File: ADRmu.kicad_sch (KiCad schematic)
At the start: 7 parts, among them J1 DIN41612_02x16_AC_EvenPins, J2 10Vf, J3 10Vs, J4 ADR, J6 LoSense, J7 GNDf

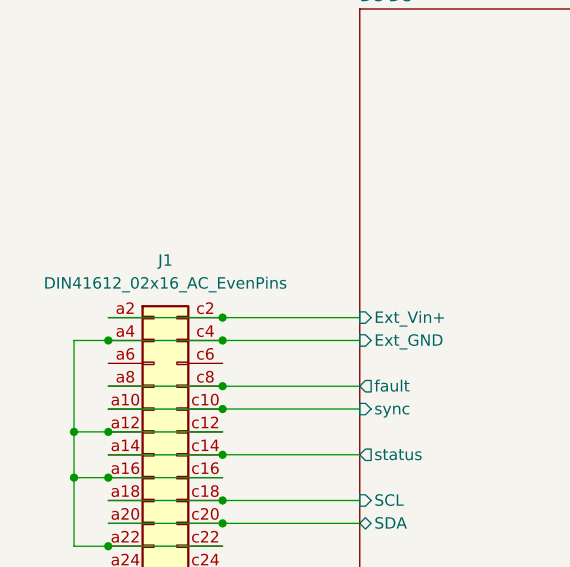
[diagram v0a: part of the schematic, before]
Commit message: schematics updated to rev.2
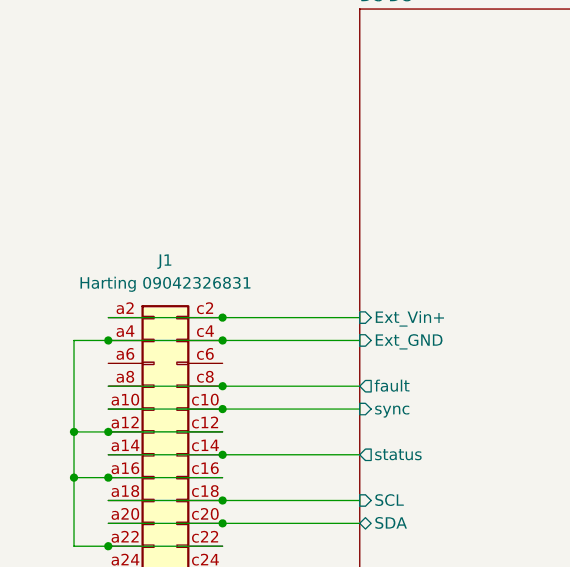
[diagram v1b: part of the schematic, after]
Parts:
- J1: value DIN41612_02x16_AC_EvenPins -> Harting 09042326831
- J2, J3, J4, J6, J7: now left out of the parts list
- SYM101: value SYM_Earth_Protective_Large -> OSMU; now left out of the parts list
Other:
- company: (none) -> RPG
- title: (none) -> Parent schematic

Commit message: asdf
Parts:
- added D101: SMAJ10CA-13-F, Diode_SMD:D_SMA, symbol Device:D_TVS
- renumbered J1 to J101, J2 to J102, J3 to J103, J4 to J104, J6 to J105, J7 to J106
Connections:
- net DC-DC/GNDf: now also D101.1 (A1)
- net ref/10Vforce: now also D101.2 (A2)

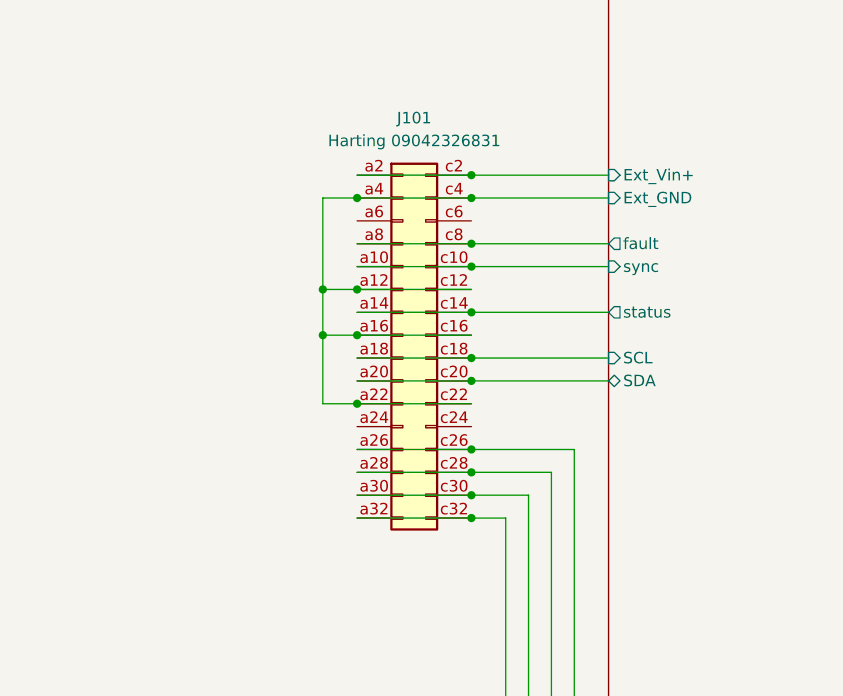
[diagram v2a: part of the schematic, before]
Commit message: adding prec resistor alternatives
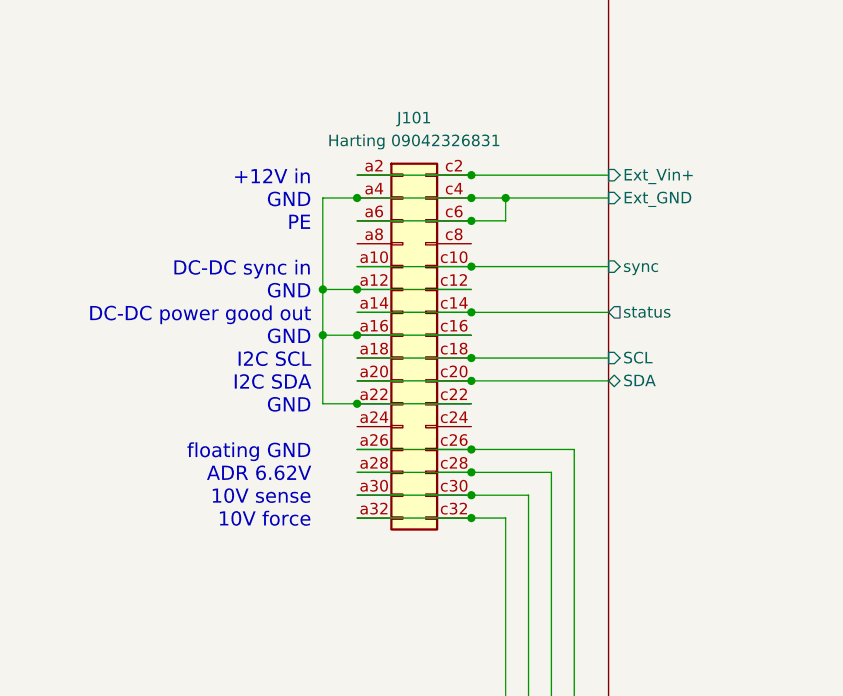
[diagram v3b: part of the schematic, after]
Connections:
- net DC-DC/Ext_GND: now also J101.a6 (Pin_a6), J101.c6 (Pin_c6)
- net DC-DC/fault: no longer names the net of J101.a8 (Pin_a8)
- net DC-DC/fault: no longer J101.c8 (Pin_c8)
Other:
- sheet DC-DC ports: added none; removed fault
- note added: "+12V in GND PE DC-DC sync in GND DC-DC power good out GND I2C SCL I2C SDA GND floating GND ADR 6.62V 10V sense 10V force"

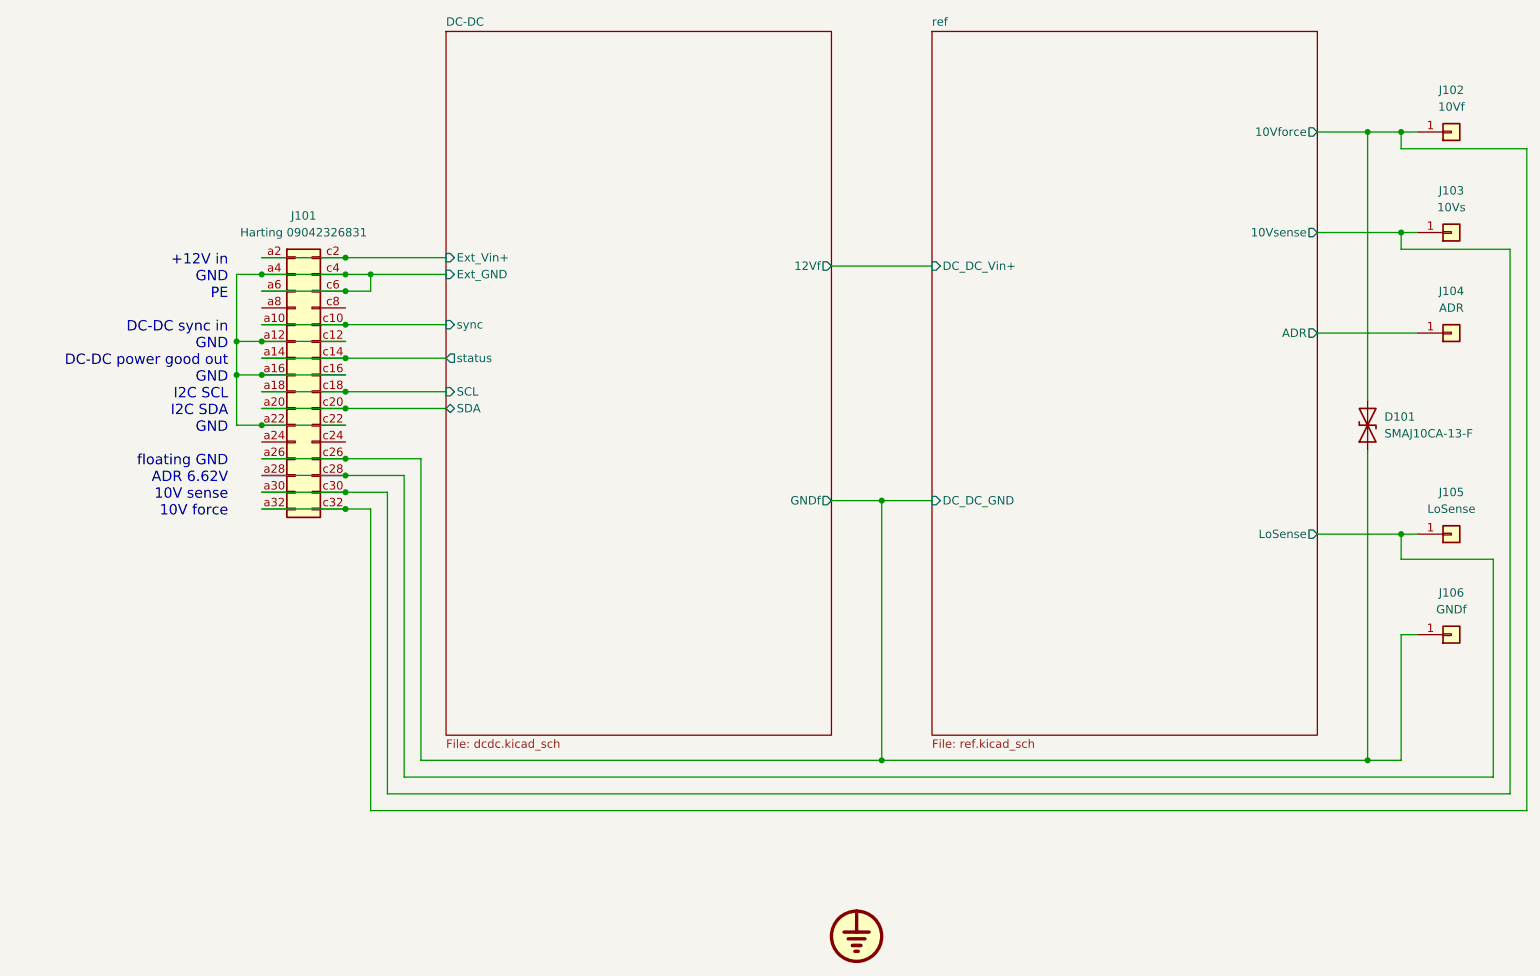
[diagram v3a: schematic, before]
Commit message: goodbye proto area, hello resistor networks
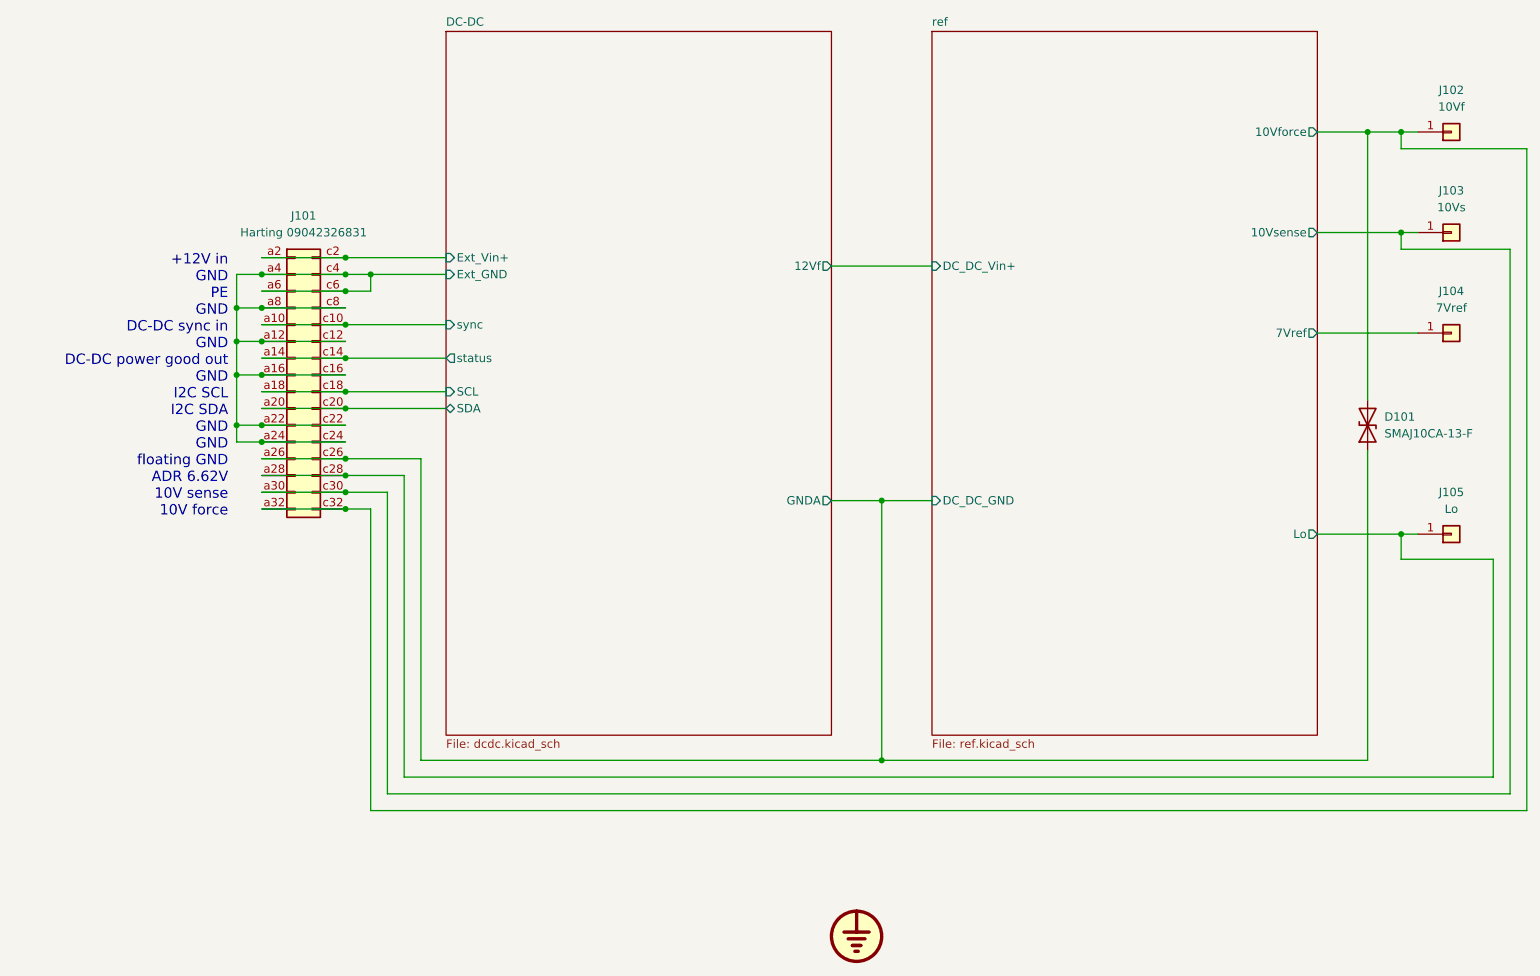
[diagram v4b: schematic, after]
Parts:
- removed J106: GNDf, Connector_Wire:SolderWire-1sqmm_1x01_D1.4mm_OD3.9mm, symbol Connector_Generic:Conn_01x01
- J104: value ADR -> 7Vref
- J105: value LoSense -> Lo
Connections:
- net DC-DC/Ext_GND: now also J101.a24 (Pin_a24), J101.a8 (Pin_a8), J101.c24 (Pin_c24), J101.c8 (Pin_c8)
- net DC-DC/GNDf renamed DC-DC/GNDA
- net ref/ADR renamed ref/7Vref
- net ref/LoSense renamed ref/Lo
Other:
- sheet DC-DC ports: added GNDA; removed GNDf
- sheet ref ports: added 7Vref, Lo; removed ADR, LoSense
- note added: "+12V in GND PE GND DC-DC sync in GND DC-DC power good out GND I2C SCL I2C SDA GND GND floating GND ADR 6.62V 10V sense 10V force"
- note removed: "+12V in GND PE DC-DC sync in GND DC-DC power good out GND I2C SCL I2C SDA GND floating GND ADR 6.62V 10V sense 10V force"

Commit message: Rev 0.3
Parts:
- removed D101: SMAJ10CA-13-F, Diode_SMD:D_SMA, symbol Device:D_TVS
- added D101: SMAJ11A‎, Diode_SMD:D_SMA, symbol Device:D_Zener
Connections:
- net DC-DC/GNDA: now also D101.2 (A)
- net ref/10Vforce: now also D101.1 (K)
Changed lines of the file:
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@@
   (title_block
     (title "Parent schematic")
-    (date "2022-02-02")
-    (rev "0.2")
+    (date "2022-02-11")
+    (rev "0.3")
     (company "RPG")
     (comment 1 "All resistors 0.1% MF unless otherwise noted")
@@
     (at 50.8 114.3 0)
     (effects (font (size 1.5748 1.5748)) (justify right bottom))
+  )
+  (symbol (lib_id "Device:D_Zener") (at 223.52 100.33 270) (unit 1)
+    (in_bom yes) (on_board yes) (fields_autoplaced)
+    (property "Reference" "D101" (id 0) (at 226.06 99.0599 90)
+      (effects (font (size 1.27 1.27)) (justify left))
+    )
+    (property "Value" "SMAJ11A‎" (id 1) (at 226.06 101.5999 90)
+      (effects (font (size 1.27 1.27)) (justify left))
+    )
+    (property "Footprint" "Diode_SMD:D_SMA" (id 2) (at 223.52 100.33 0)
+      (effects (font (size 1.27 1.27)) hide)
+    )
+    (property "Datasheet" "~" (id 3) (at 223.52 100.33 0)
+      (effects (font (size 1.27 1.27)) hide)
+    )
+    (pin "1")
+    (pin "2")
   )
   (symbol (lib_id "Connector_Generic:Conn_01x01") (at 236.22 86.36 0) (mirror x) (unit 1)
@@
     )
     (pin "1")
-  )
-  (symbol (lib_id "Device:D_TVS") (at 223.52 100.33 90) (unit 1)
-    (in_bom yes) (on_board yes) (fields_autoplaced)
-    (property "Reference" "D101" (id 0) (at 226.06 99.0599 90)
-      (effects (font (size 1.27 1.27)) (justify right))
-    )
-    (property "Value" "SMAJ10CA-13-F" (id 1) (at 226.06 101.5999 90)
-      (effects (font (size 1.27 1.27)) (justify right))
-    )
-    (property "Footprint" "Diode_SMD:D_SMA" (id 2) (at 223.52 100.33 0)
-      (effects (font (size 1.27 1.27)) hide)
-    )
-    (property "Datasheet" "~" (id 3) (at 223.52 100.33 0)
-      (effects (font (size 1.27 1.27)) hide)
-    )
-    (pin "1")
-    (pin "2")
   )
   (symbol (lib_id "Connector_Generic:Conn_01x01") (at 236.22 71.12 0) (mirror x) (unit 1)
@@
       (reference "C313") (unit 1) (value "22u 25V") (footprint "Capacitor_SMD:C_1206_3216Metric")
     )
-    (path "/4730213f-fecd-4d57-8774-30198ac3be94"
-      (reference "D101") (unit 1) (value "SMAJ10CA-13-F") (footprint "Diode_SMD:D_SMA")
+    (path "/0e9b9904-0b79-4bc6-87d8-b85af87fe8cd"
+      (reference "D101") (unit 1) (value "SMAJ11A‎") (footprint "Diode_SMD:D_SMA")
     )
     (path "/027929a1-62dd-40f4-83d4-39d0de3b1543/fe2c9782-2ff0-473c-98b0-ea9a985143fb"
